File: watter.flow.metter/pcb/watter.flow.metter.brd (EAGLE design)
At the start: 131.9 x 48.2 mm, 25 parts, among them Q1 BC546A

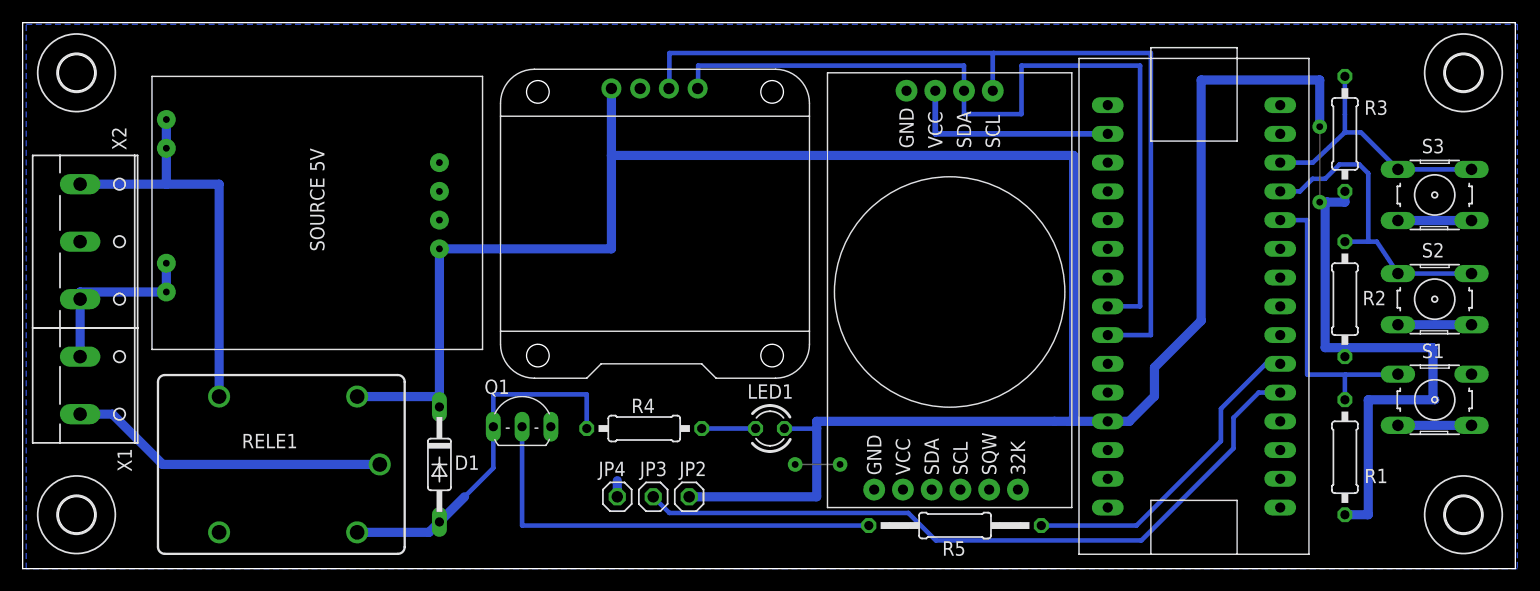
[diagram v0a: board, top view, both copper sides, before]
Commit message: clock with dimmer and date switching
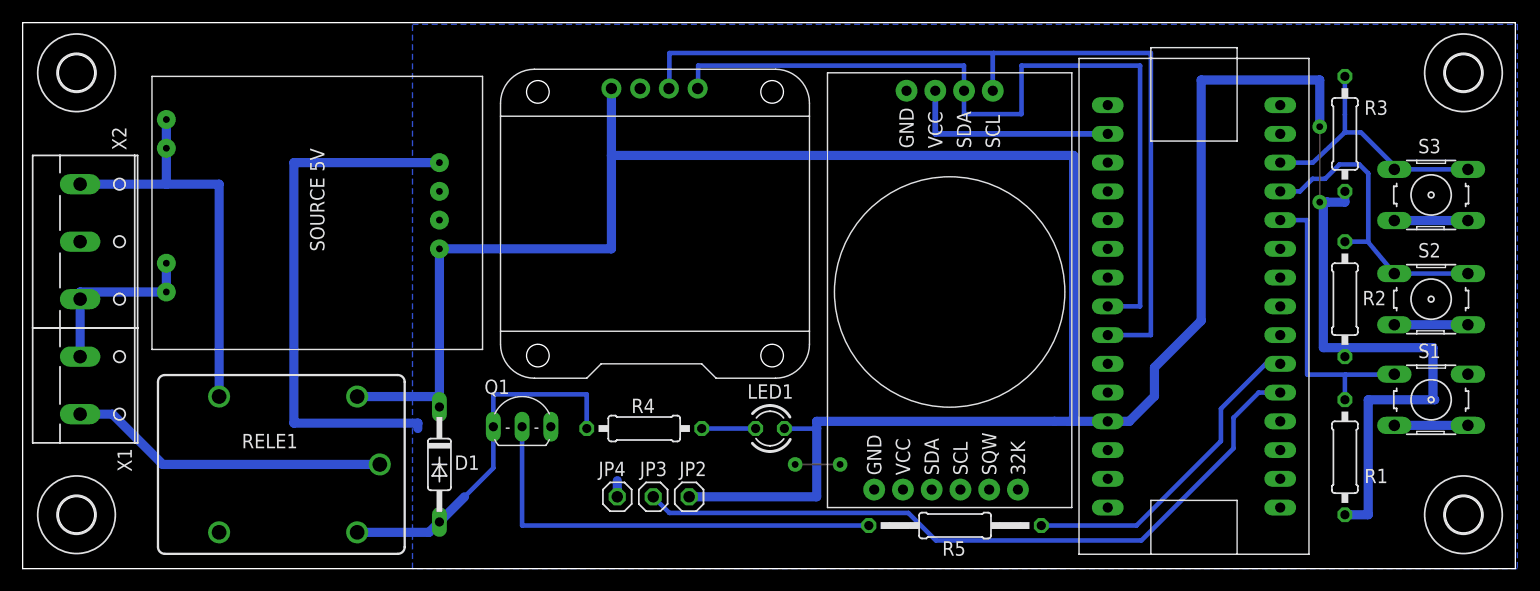
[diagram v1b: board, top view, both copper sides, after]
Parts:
- moved S1 0.32 mm to (124.5, 14.9)
- moved S2 0.32 mm to (124.5, 23.8)
- moved S3 0.32 mm to (124.5, 33.0)
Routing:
- net GND: track 25.0 -> 72.3 mm
